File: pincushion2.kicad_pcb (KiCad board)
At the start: 2 copper layers, 101.6 x 101.6 mm, 120 parts, among them IC1 AD633JN, IC2 AD633JN, J1 Conn_01x03_Male, J2 Conn_01x03_Male, J3 Conn_01x03_Male, J4 Conn_01x03_Male, J5 Conn_01x03_Male, J6 640385-4, J7 640385-4, U1 TL082, U2 TL082, U3 TL082, U4 TL082, U5 TL082, U6 TL082, U7 DI78L09ZAB, U8 MCP1702-1502E/TO, U9 DI79L09ZAB

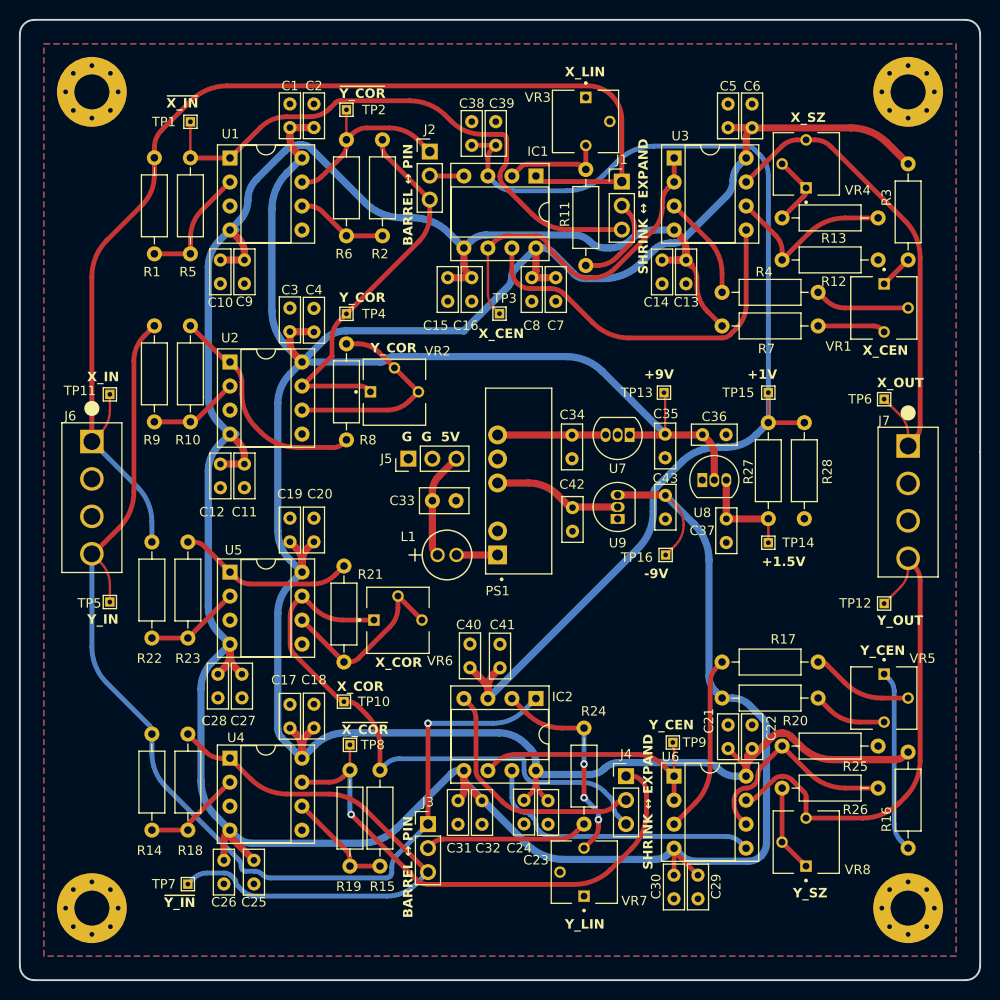
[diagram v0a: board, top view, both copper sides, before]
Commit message: move input connector so board can stack with the sega-amplifone board
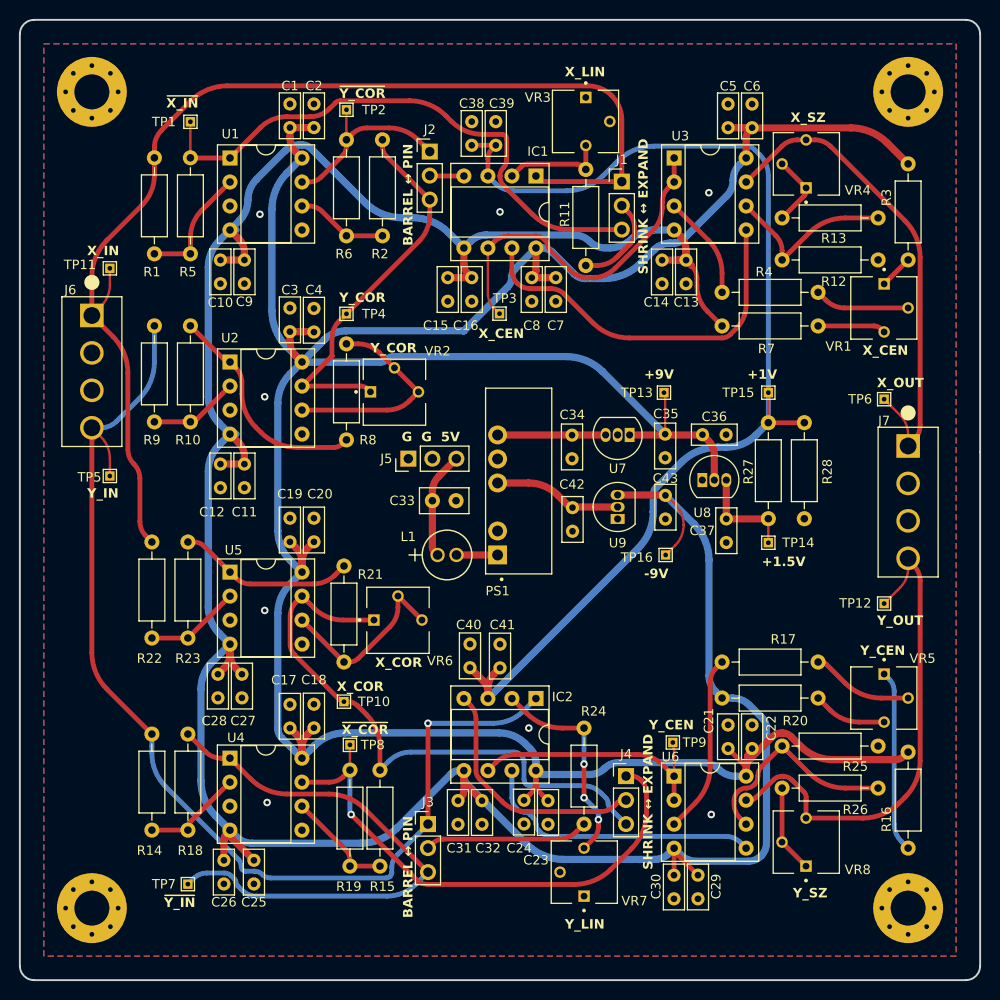
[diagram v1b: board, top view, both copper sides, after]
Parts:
- moved J6 13.3 mm to (27.9, 51.6)
- moved TP5 13.3 mm to (29.8, 68.6)
- moved TP11 13.3 mm to (29.8, 46.6)
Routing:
- net X_IN: track 122.4 -> 120.7 mm
- net Y_IN: track 117.6 -> 119.0 mm
- net /amps-y/X_COR: track 61.6 -> 62.4 mm
- net GND: vias 0 -> 8

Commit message: add thermals to caps and resistors. more pitch spacing for inductor and TO92 packages.
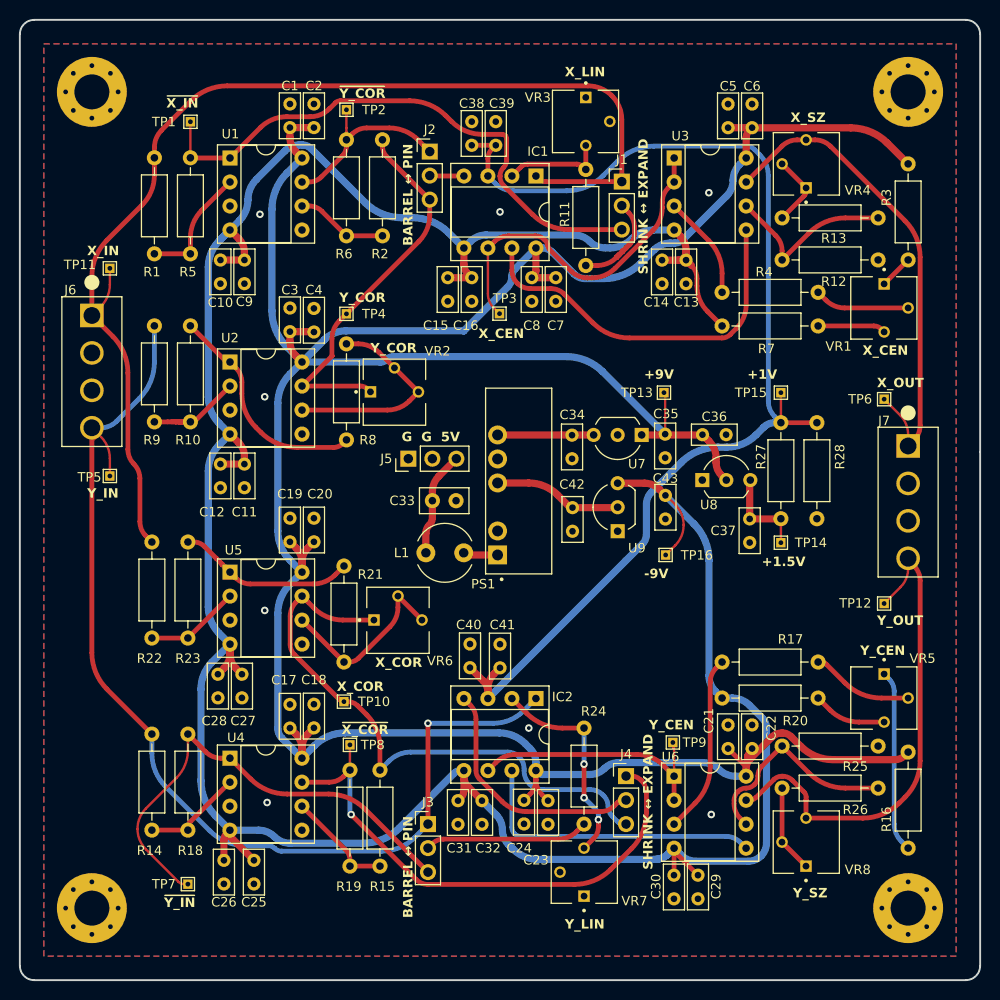
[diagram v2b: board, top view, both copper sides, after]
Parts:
- L1: footprint digikey-11R223C:1100R_MUR -> Inductor_THT:L_Radial_D6.0mm_P4.00mm
- U7, U8, U9: footprint Package_TO_SOT_THT:TO-92_Inline -> Package_TO_SOT_THT:TO-92_Inline_Wide
- moved C37 2.47 mm to (97.5, 73.1)
- moved R27 1.33 mm to (100.8, 62.9)
- moved R28 1.33 mm to (104.6, 73.1)
- moved TP14 1.33 mm to (100.8, 75.6)
- moved TP15 1.33 mm to (100.8, 59.8)
- moved U9 1.30 mm to (83.6, 74.4)
- moved U7 1.27 mm to (86.1, 64.2)
- moved L1 1.26 mm to (63.3, 76.7)
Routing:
- net /amps-y/~{Y_IN}: track 58.5 -> 51.0 mm
- net -9V: track 309.2 -> 302.2 mm
- net Y_IN: track 119.0 -> 113.4 mm
- net +9V: track 330.0 -> 327.3 mm
- net /amps-x/X_CEN: track 37.3 -> 35.6 mm
- net Net-(IC2-W): track 30.2 -> 31.7 mm
- net Net-(R21-Pad1): track 18.8 -> 17.3 mm
- net /amps-y/~{X_COR}: track 56.1 -> 54.7 mm
- net +12V: track 11.4 -> 10.2 mm
- net +1V5: track 11.1 -> 9.90 mm
- net Net-(PS1-+VIN): track 4.35 -> 3.20 mm
- net X_OUT: track 52.0 -> 51.1 mm
- net Net-(U2A--): track 9.55 -> 8.83 mm
- net Net-(R10-Pad2): track 23.9 -> 23.2 mm
- net /amps-y/X_COR: track 62.4 -> 61.8 mm
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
